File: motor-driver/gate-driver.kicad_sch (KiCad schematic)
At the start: 17 parts, among them U9 FAN7388

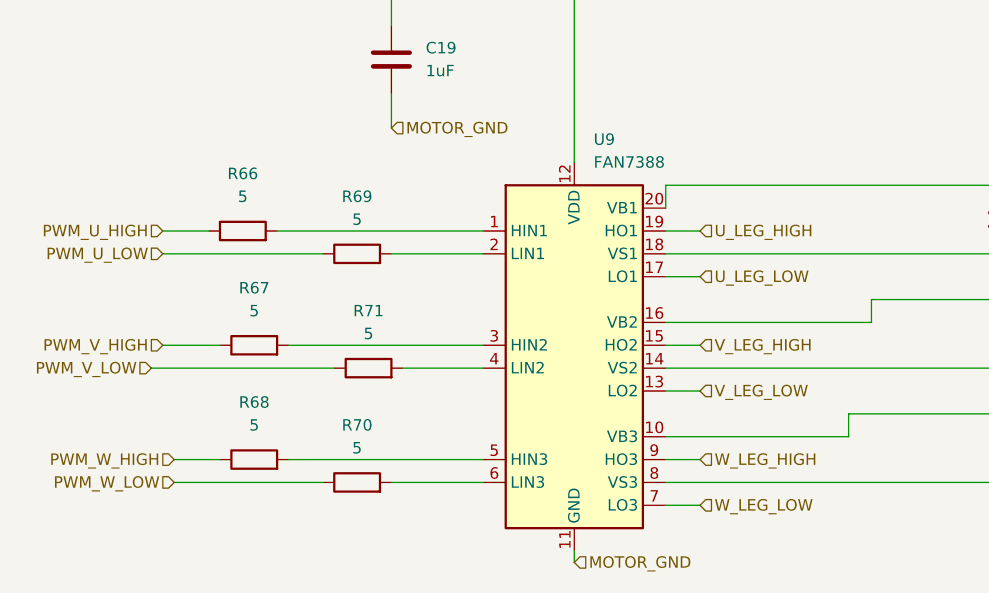
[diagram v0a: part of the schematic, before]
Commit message: added connectors starting pcb layout
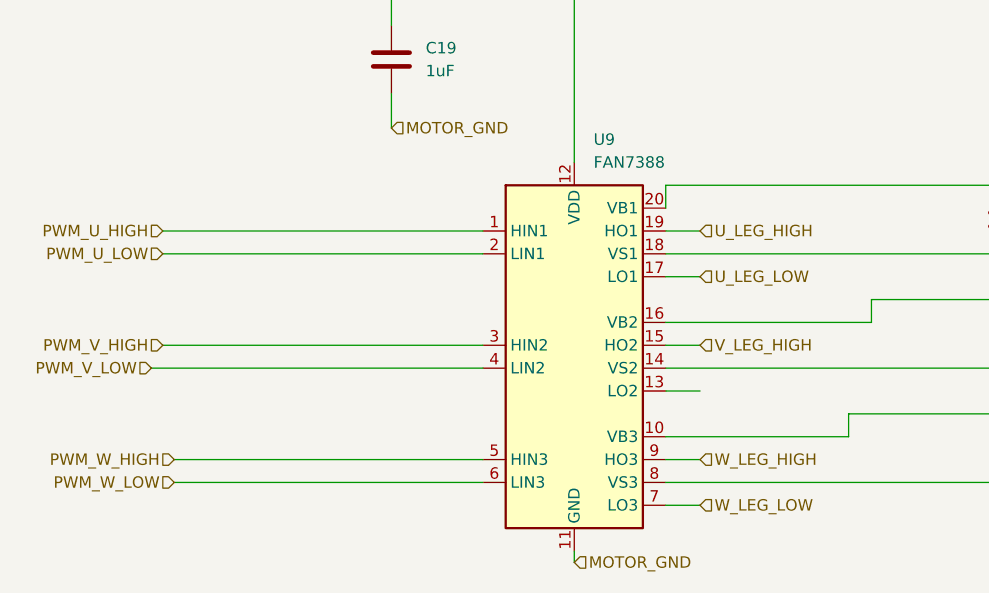
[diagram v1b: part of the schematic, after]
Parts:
- removed R66, R67, R68, R69, R70, R71: 5, symbol Device:R
- C19: footprint Capacitor_SMD:C_0603_1608Metric_Pad1.08x0.95mm_HandSolder -> Capacitor_SMD:C_0805_2012Metric
- C20, C21, C22: footprint Capacitor_SMD:C_0201_0603Metric_Pad0.64x0.40mm_HandSolder -> Capacitor_SMD:C_0805_2012Metric
- D1, D2, D3: footprint Diode_SMD:D_0201_0603Metric_Pad0.64x0.40mm_HandSolder -> Diode_SMD:D_0805_2012Metric
- R72, R73, R74: footprint (none) -> Resistor_SMD:R_0805_2012Metric
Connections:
- net PWM_U_HIGH: now also U9.1 (HIN1)
- net PWM_U_LOW: now also U9.2 (LIN1)
- net PWM_V_HIGH: now also U9.3 (HIN2)
- net PWM_V_LOW: now also U9.4 (LIN2)
- net PWM_W_HIGH: now also U9.5 (HIN3)
- net PWM_W_LOW: now also U9.6 (LIN3)
- net V_LEG_LOW: no longer names the net of U9.13 (LO2)

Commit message: commit before changing custom sullen key sense
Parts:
- C19, C20, C21, C22: footprint Capacitor_SMD:C_0805_2012Metric -> Capacitor_SMD:C_0603_1608Metric
- R72, R73, R74: footprint Resistor_SMD:R_0805_2012Metric -> Resistor_SMD:R_0603_1608Metric
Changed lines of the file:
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@@
 			)
 		)
-		(property "Footprint" "Resistor_SMD:R_0805_2012Metric"
+		(property "Footprint" "Resistor_SMD:R_0603_1608Metric"
 			(at 148.082 48.26 90)
 			(effects
@@
 			)
 		)
-		(property "Footprint" "Capacitor_SMD:C_0805_2012Metric"
+		(property "Footprint" "Capacitor_SMD:C_0603_1608Metric"
 			(at 203.5048 90.17 0)
 			(effects
@@
 			)
 		)
-		(property "Footprint" "Resistor_SMD:R_0805_2012Metric"
+		(property "Footprint" "Resistor_SMD:R_0603_1608Metric"
 			(at 173.482 52.07 90)
 			(effects
@@
 			)
 		)
-		(property "Footprint" "Capacitor_SMD:C_0805_2012Metric"
+		(property "Footprint" "Capacitor_SMD:C_0603_1608Metric"
 			(at 148.8948 64.77 0)
 			(effects
@@
 			)
 		)
-		(property "Footprint" "Capacitor_SMD:C_0805_2012Metric"
+		(property "Footprint" "Capacitor_SMD:C_0603_1608Metric"
 			(at 82.2452 54.61 0)
 			(effects
@@
 			)
 		)
-		(property "Footprint" "Resistor_SMD:R_0805_2012Metric"
+		(property "Footprint" "Resistor_SMD:R_0603_1608Metric"
 			(at 209.042 52.07 90)
 			(effects
@@
 			)
 		)
-		(property "Footprint" "Capacitor_SMD:C_0805_2012Metric"
+		(property "Footprint" "Capacitor_SMD:C_0603_1608Metric"
 			(at 166.6748 77.47 0)
 			(effects

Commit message: post revisions
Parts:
- renumbered C19 to C1, C20 to C14, C21 to C15, C22 to C44, D1 to D4, D2 to D5, D3 to D6, R74 to R100, R72 to R98, R73 to R99, U9 to U17
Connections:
- net V_GATE_L: now reaches U17.13 (LO2)
- net MOTOR_GND renamed GND
- net U_LEG_HIGH renamed U_GATE_H
- net U_LEG_LOW renamed U_GATE_L
- net V_LEG_HIGH renamed V_GATE_H
- net W_LEG_HIGH renamed W_GATE_H
- net W_LEG_LOW renamed W_GATE_L
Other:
- note added: "Bootstrap capacitors are selected with 20-40 kHz PWM"
- company: (none) -> Drone 
- moved on the sheet: C1, C44

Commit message: routing complete
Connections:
- net PWM_U_HIGH: now also U17.5 (HIN3); no longer U17.1 (HIN1)
- net PWM_U_LOW: now also U17.6 (LIN3); no longer U17.2 (LIN1)
- net PWM_W_HIGH: now also U17.1 (HIN1); no longer U17.5 (HIN3)
- net PWM_W_LOW: now also U17.2 (LIN1); no longer U17.6 (LIN3)
- net U_GATE_H: now also U17.9 (HO3); no longer U17.19 (HO1)
- net U_GATE_L: now also U17.7 (LO3); no longer U17.17 (LO1)
- net U_LEG_BST: now also C44.1, U17.8 (VS3); no longer C14.1, U17.18 (VS1)
- net W_GATE_H: now also U17.19 (HO1); no longer U17.9 (HO3)
- net W_GATE_L: now also U17.17 (LO1); no longer U17.7 (LO3)
- net W_LEG_BST: now also C14.1, U17.18 (VS1); no longer C44.1, U17.8 (VS3)
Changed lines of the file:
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@@
+		)
+	)
+	(hierarchical_label "PWM_U_HIGH"
+		(shape input)
+		(at 57.15 95.25 180)
+		(effects
+			(font
+				(size 1.27 1.27)
+			)
+			(justify right)
+		)
+	)
+	(hierarchical_label "U_GATE_H"
+		(shape input)
+		(at 115.57 95.25 0)
+		(effects
+			(font
+				(size 1.27 1.27)
+			)
+			(justify left)
 		)
 	)
 	(hierarchical_label "W_GATE_H"
 		(shape input)
-		(at 115.57 95.25 0)
+		(at 115.57 69.85 0)
+		(effects
+			(font
+				(size 1.27 1.27)
+			)
+			(justify left)
+		)
+	)
+	(hierarchical_label "V_GATE_L"
+		(shape input)
+		(at 115.57 87.63 0)
+		(effects
+			(font
+				(size 1.27 1.27)
+			)
+			(justify left)
+		)
+	)
+	(hierarchical_label "PWM_W_LOW"
+		(shape input)
+		(at 55.88 72.39 180)
+		(effects
+			(font
+				(size 1.27 1.27)
+			)
+			(justify right)
+		)
+	)
+	(hierarchical_label "PWM_W_HIGH"
+		(shape input)
+		(at 55.88 69.85 180)
+		(effects
+			(font
+				(size 1.27 1.27)
+			)
+			(justify right)
+		)
+	)
+	(hierarchical_label "W_GATE_L"
+		(shape input)
+		(at 115.57 74.93 0)
+		(effects
+			(font
+				(size 1.27 1.27)
+			)
+			(justify left)
+		)
+	)
+	(hierarchical_label "U_LEG_BST"
+		(shape input)
+		(at 210.82 97.79 0)
+		(effects
+			(font
+				(size 1.27 1.27)
+			)
+			(justify left)
+		)
+	)
+	(hierarchical_label "U_GATE_L"
+		(shape input)
+		(at 115.57 100.33 0)
 		(effects
 			(font
@@
 		)
 	)
-	(hierarchical_label "PWM_W_LOW"
+	(hierarchical_label "PWM_V_HIGH"
+		(shape input)
+		(at 55.88 82.55 180)
+		(effects
+			(font
+				(size 1.27 1.27)
+			)
+			(justify right)
+		)
+	)
+	(hierarchical_label "PWM_U_LOW"
 		(shape input)
 		(at 57.15 97.79 180)
@@
 		)
 	)
-	(hierarchical_label "U_GATE_H"
+	(hierarchical_label "V_GATE_H"
 		(shape input)
-		(at 115.57 69.85 0)
+		(at 115.57 82.55 0)
+		(effects
+			(font
+				(size 1.27 1.27)
+			)
+			(justify left)
+		)
+	)
+	(hierarchical_label "W_LEG_BST"
+		(shape input)
+		(at 160.02 72.39 0)
 		(effects
 			(font
@@
 		)
 	)
-	(hierarchical_label "U_GATE_L"
-		(shape input)
-		(at 115.57 74.93 0)
-		(effects
-			(font
-				(size 1.27 1.27)
-			)
-			(justify left)
-		)
-	)
-	(hierarchical_label "PWM_W_HIGH"
-		(shape input)
-		(at 57.15 95.25 180)
-		(effects
-			(font
-				(size 1.27 1.27)
-			)
-			(justify right)
-		)
-	)
-	(hierarchical_label "PWM_V_HIGH"
-		(shape input)
-		(at 55.88 82.55 180)
-		(effects
-			(font
-				(size 1.27 1.27)
-			)
-			(justify right)
-		)
-	)
-	(hierarchical_label "W_GATE_L"
-		(shape input)
-		(at 115.57 100.33 0)
-		(effects
-			(font
-				(size 1.27 1.27)
-			)
-			(justify left)
-		)
-	)
-	(hierarchical_label "PWM_U_LOW"
-		(shape input)
-		(at 55.88 72.39 180)
-		(effects
-			(font
-				(size 1.27 1.27)
-			)
-			(justify right)
-		)
-	)
-	(hierarchical_label "U_LEG_BST"
-		(shape input)
-		(at 160.02 72.39 0)
-		(effects
-			(font
-				(size 1.27 1.27)
-			)
-			(justify left)
-		)
-	)
-	(hierarchical_label "PWM_U_HIGH"
-		(shape input)
-		(at 55.88 69.85 180)
-		(effects
-			(font
-				(size 1.27 1.27)
-			)
-			(justify right)
-		)
-	)
-	(hierarchical_label "V_GATE_H"
-		(shape input)
-		(at 115.57 82.55 0)
-		(effects
-			(font
-				(size 1.27 1.27)
-			)
-			(justify left)
-		)
-	)
-	(hierarchical_label "V_GATE_L"
-		(shape input)
-		(at 115.57 87.63 0)
-		(effects
-			(font
-				(size 1.27 1.27)
-			)
-			(justify left)
-		)
-	)
-	(hierarchical_label "W_LEG_BST"
-		(shape input)
-		(at 210.82 97.79 0)
-		(effects
-			(font
-				(size 1.27 1.27)
-			)
-			(justify left)
-		)
-	)

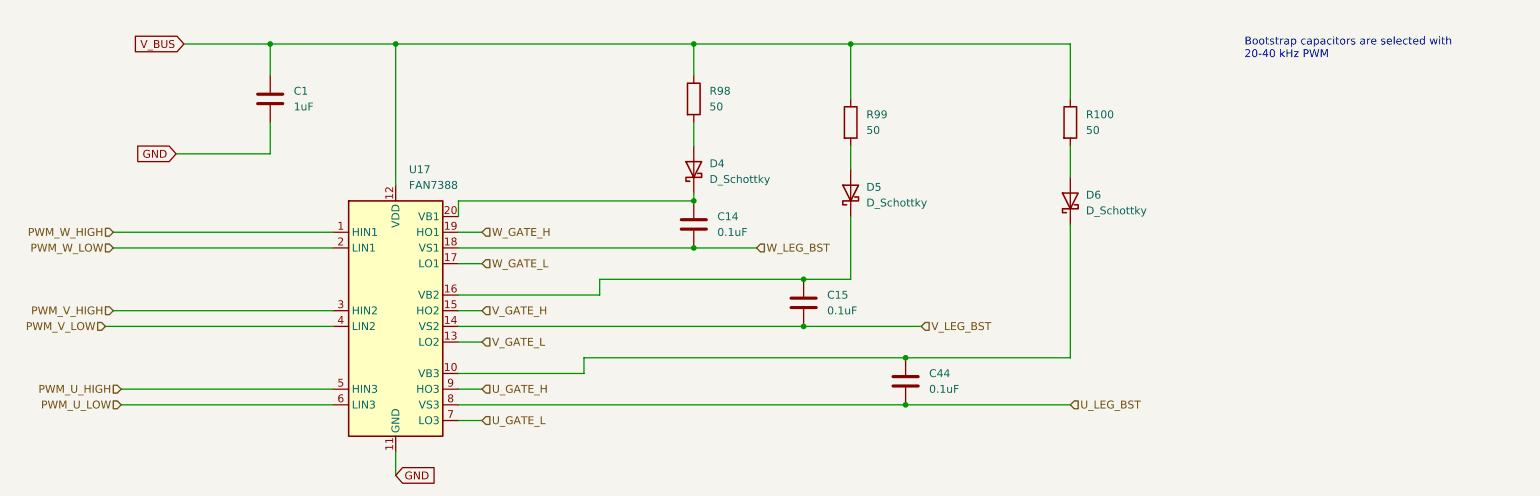
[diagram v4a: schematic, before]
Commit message: added spi connection
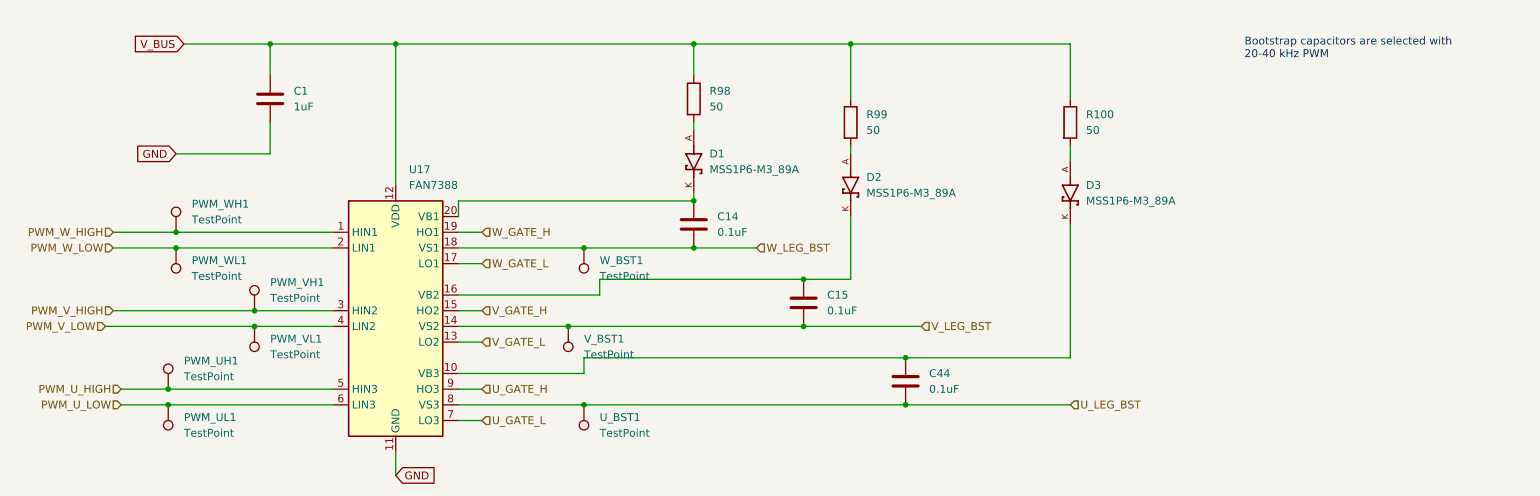
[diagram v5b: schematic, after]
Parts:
- removed D4, D5, D6: D_Schottky, Diode_SMD:D_0805_2012Metric, symbol Device:D_Schottky
- added D1, D2, D3: MSS1P6-M3_89A, MSS1P6-M3_89A:DIO_MSS1P6-M3_89A, symbol MSS1P6-M3_89A:MSS1P6-M3_89A
- added PWM_UH1, PWM_UL1, PWM_VH1, PWM_VL1, PWM_WH1, PWM_WL1, U_BST1, V_BST1, W_BST1: TestPoint, TestPoint:TestPoint_Loop_D1.80mm_Drill1.0mm_Beaded, symbol Connector:TestPoint
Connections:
- net PWM_U_HIGH: now also PWM_UH1.1
- net PWM_U_LOW: now also PWM_UL1.1
- net PWM_V_HIGH: now also PWM_VH1.1
- net PWM_V_LOW: now also PWM_VL1.1
- net PWM_W_HIGH: now also PWM_WH1.1
- net PWM_W_LOW: now also PWM_WL1.1
- net U_LEG_BST: now also U_BST1.1
- net V_LEG_BST: now also V_BST1.1
- net W_LEG_BST: now also W_BST1.1
- net at R98.2: now also D1.A
- net at C44.2, U17.10 (VB3): now also D3.K
- net at R99.2: now also D2.A
- net at C15.2, U17.16 (VB2): now also D2.K
- net at C14.2, U17.20 (VB1): now also D1.K
- net at R100.2: now also D3.A

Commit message: added test points
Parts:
- removed PWM_UH1, PWM_UL1, PWM_VH1, PWM_VL1, PWM_WH1, PWM_WL1, U_BST1, V_BST1, W_BST1: TestPoint, TestPoint:TestPoint_Loop_D1.80mm_Drill1.0mm_Beaded, symbol Connector:TestPoint

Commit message: bom finished
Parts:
- C1: value 1uF -> 1u; MANUFACTURER (none) -> KEMET; MPN (none) -> C0603C105K4RACTU; Supplier (none) -> Digikey
- C14, C15, C44: value 0.1uF -> 0.1u; MANUFACTURER (none) -> KEMET; MPN (none) -> C0603C104K5RACTU; Supplier (none) -> Digikey
- D1, D2, D3: Availability In Stock -> (none); CREATOR DIZAR -> (none); Check_prices https://www.snapeda.com/parts/MSS1P6-M3/89A/Vishay/view-par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 -> (none); Description_1 Diode,Schottky Barrier,Vr 60V,If 1A,Pkg MicroSMP,Vf 0.52V,C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 -> (none); MPN (none) -> MSS1P6-M3/89A; Supplier (none) -> Digikey
- R100, R98, R99: value 50 -> 33; MANUFACTURER (none) -> YAGEO; MPN (none) -> RC0603FR-0733RL; Supplier (none) -> Digikey
- U17: MANUFACTURER (none) -> onsemi; MPN (none) -> FAN7388MX; Supplier (none) -> Digikey
